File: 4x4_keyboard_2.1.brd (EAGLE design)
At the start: 69.5 x 142.2 mm, 74 parts, among them U2 AMS1117-5.0

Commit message: Routing compelte of uc
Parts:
- moved SV2 3.16 mm to (4.17, 132.3)
- moved LED1 2.37 mm to (20.4, 116.7)
- moved R4 2.24 mm to (22.8, 116.5)
- moved C10 0.74 mm to (24.6, 116.3), turned to 270 degrees
- moved C5 0.62 mm to (28.2, 133.6)
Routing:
- net VCC: track 0.00 -> 82.8 mm
- net SW1: track 0.00 -> 48.9 mm, vias 0 -> 4
- net A1: track 0.00 -> 48.8 mm, vias 0 -> 2
- net A2: track 0.00 -> 47.0 mm, vias 0 -> 4
- net B1: track 0.00 -> 46.9 mm, vias 0 -> 2
- net B2: track 0.00 -> 46.7 mm, vias 0 -> 4
- net RESET: track 0.00 -> 46.5 mm
- net SW3: track 0.00 -> 35.9 mm, vias 0 -> 1
- net SW2: track 0.00 -> 32.4 mm, vias 0 -> 1
- net MISO: track 0.00 -> 27.7 mm, vias 0 -> 2
- net SCK: track 0.00 -> 26.4 mm, vias 0 -> 2
- net MOSI: track 0.00 -> 25.8 mm, vias 0 -> 2
- net V_USB: track 0.00 -> 22.4 mm
- net N$24: track 0.00 -> 17.1 mm
- net N$27: track 0.00 -> 16.7 mm
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
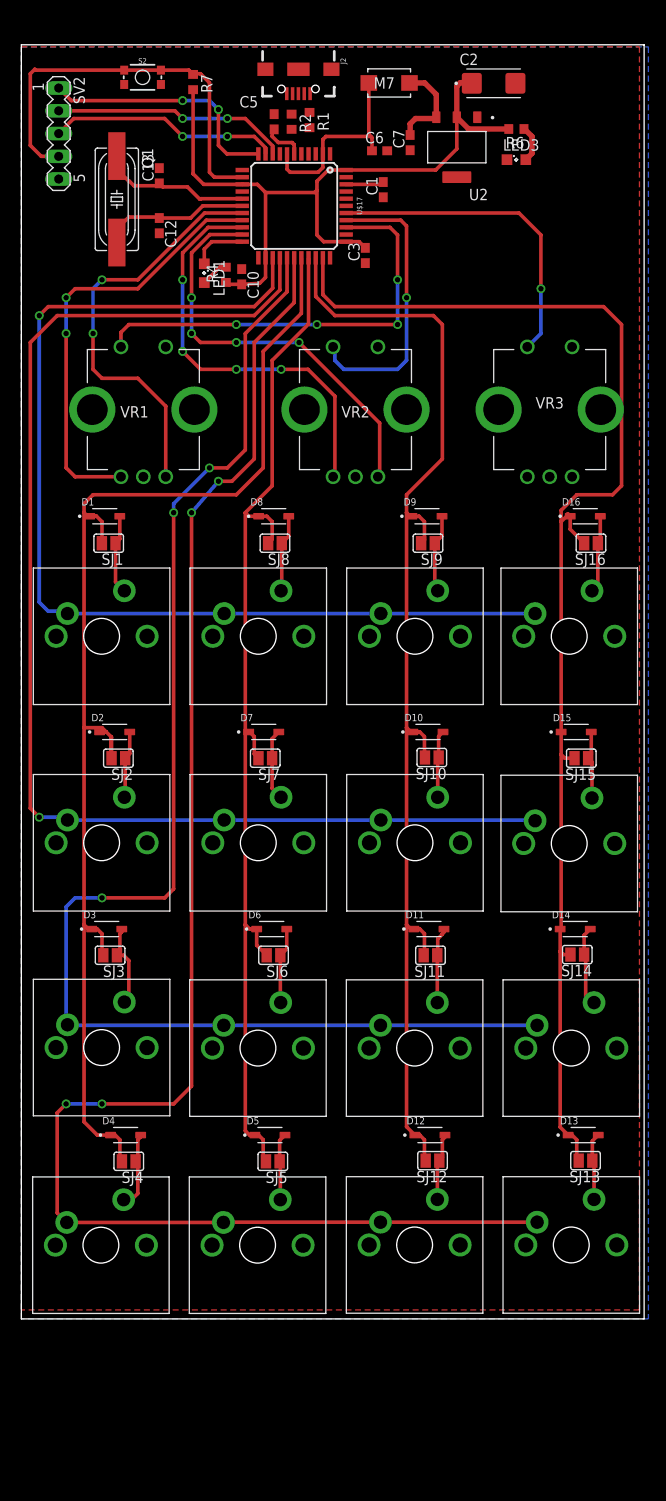
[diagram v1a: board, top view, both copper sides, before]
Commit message: Correct routing signal
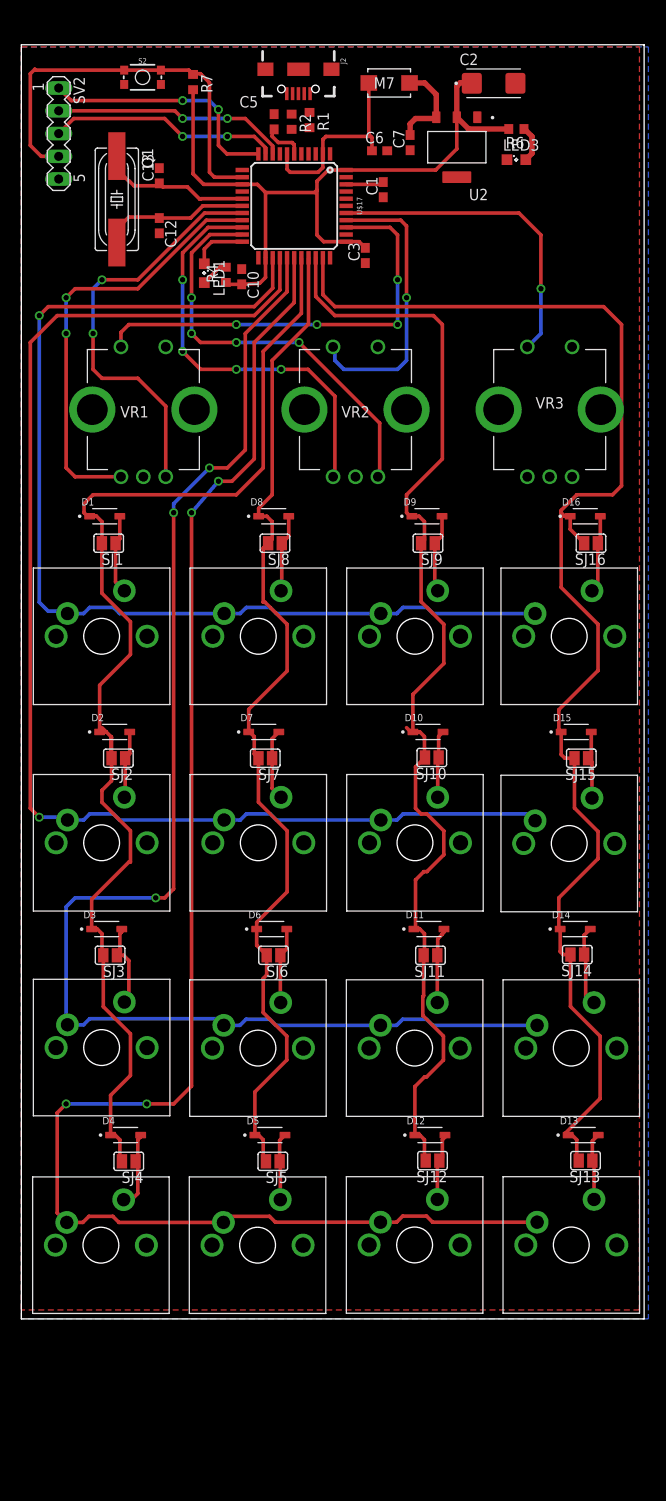
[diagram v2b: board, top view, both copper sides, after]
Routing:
- net COL4: track 146.6 -> 154.9 mm
- net COL1: track 142.0 -> 136.5 mm
- net COL2: track 119.6 -> 114.9 mm
- net COL3: track 130.9 -> 129.2 mm
- net ROW1: track 118.6 -> 120.3 mm
- net ROW3: track 155.4 -> 157.1 mm
- net ROW2: track 142.8 -> 144.5 mm
- net ROW4: track 179.4 -> 181.0 mm

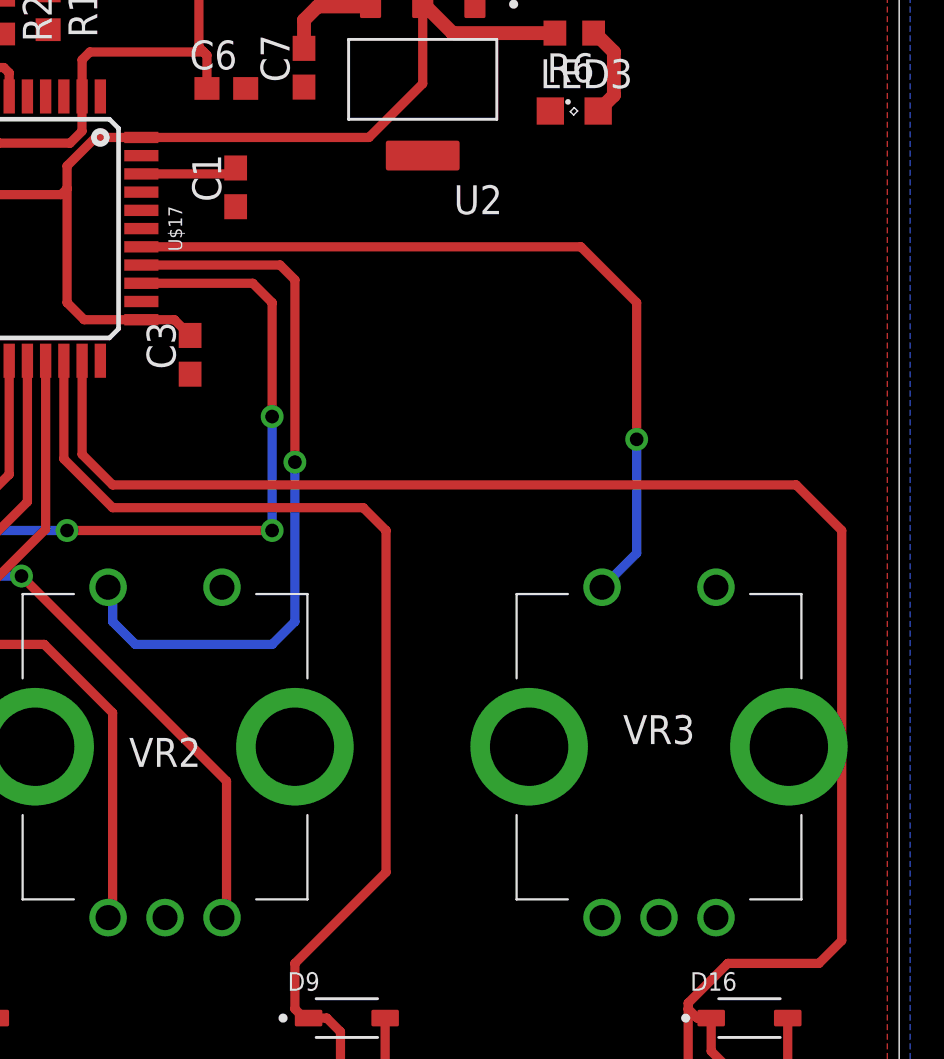
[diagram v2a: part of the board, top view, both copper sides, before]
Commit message: complete the routing of encoder and changer it analogpins
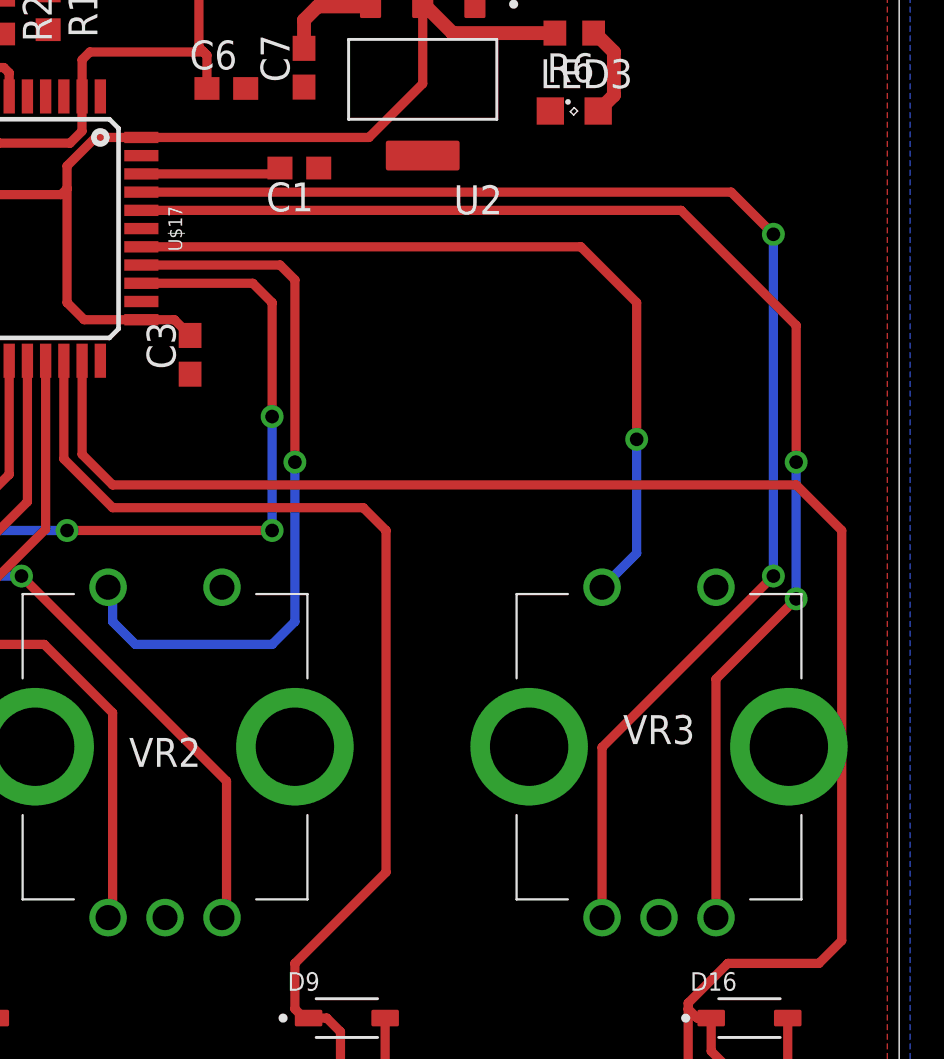
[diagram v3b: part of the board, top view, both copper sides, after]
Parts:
- moved C1 2.92 mm to (43.2, 126.9), turned to 180 degrees
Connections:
- net A3: now also U$17.41; no longer U$17.12
- net B3: now also U$17.40; no longer U$17.8
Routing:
- net A3: track 0.00 -> 61.6 mm, vias 0 -> 2
- net B3: track 0.00 -> 58.3 mm, vias 0 -> 2
- net AREF: track 4.25 -> 6.19 mm
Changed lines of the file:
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@@
 <?xml version="1.0" encoding="utf-8"?>
 <!DOCTYPE eagle SYSTEM "eagle.dtd">
-<eagle version="9.6.2">
+<eagle version="6.4">
 <drawing>
 <settings>
 <setting alwaysvectorfont="no"/>
-<setting keepoldvectorfont="yes"/>
 <setting verticaltext="up"/>
 </settings>
@@
 <param name="dpMaxLengthDifference" value="10mm"/>
 <param name="dpGapFactor" value="2.5"/>
+<param name="checkGrid" value="0"/>
 <param name="checkAngle" value="0"/>
 <param name="checkFont" value="1"/>
 <param name="checkRestrict" value="1"/>
-<param name="checkStop" value="0"/>
-<param name="checkValues" value="0"/>
-<param name="checkNames" value="1"/>
-<param name="checkWireStubs" value="1"/>
-<param name="checkPolygonWidth" value="0"/>
 <param name="useDiameter" value="13"/>
 <param name="maxErrors" value="50"/>
@@
 <pass name="Default">
 <param name="RoutingGrid" value="50mil"/>
-<param name="AutoGrid" value="1"/>
-<param name="Efforts" value="0"/>
-<param name="TopRouterVariant" value="1"/>
 <param name="tpViaShape" value="round"/>
 <param name="PrefDir.1" value="|"/>
@@
 </autorouter>
 <elements>
-<element name="C1" library="rcl" package="C0603" value="0.1uF" x="40.4" y="126.06" smashed="yes" rot="R90">
-<attribute name="NAME" x="39.765" y="125.425" size="1.27" layer="25" rot="R90"/>
-<attribute name="POPULARITY" value="73" x="142" y="154" size="1.778" layer="27" rot="R90" display="off"/>
-<attribute name="SPICEPREFIX" value="C" x="142" y="154" size="1.778" layer="27" rot="R90" display="off"/>
-<attribute name="VALUE" x="42.305" y="125.425" size="1.27" layer="27" rot="R90"/>
+<element name="C1" library="rcl" package="C0603" value="0.1uF" x="43.194" y="126.908" smashed="yes" rot="R180">
+<attribute name="NAME" x="43.829" y="126.273" size="1.27" layer="25" rot="R180"/>
+<attribute name="POPULARITY" value="73" x="15.254" y="228.508" size="1.778" layer="27" rot="R180" display="off"/>
+<attribute name="SPICEPREFIX" value="C" x="15.254" y="228.508" size="1.778" layer="27" rot="R180" display="off"/>
+<attribute name="VALUE" x="43.829" y="128.813" size="1.27" layer="27" rot="R180"/>
 </element>
 <element name="C10" library="rcl" package="C0603" value="1.0uF" x="24.6" y="116.34" smashed="yes" rot="R270">
@@
 <wire x1="30.28" y1="136.775" x2="29.63" y2="136.775" width="0" layer="19" extent="1-1"/>
 <wire x1="28.219" y1="134.49" x2="29.63" y2="136.775" width="0" layer="19" extent="1-1"/>
-<wire x1="36.26" y1="127.45" x2="40.4" y2="125.21" width="0" layer="19" extent="1-1"/>
+<wire x1="36.26" y1="127.45" x2="44.044" y2="126.908" width="0" layer="19" extent="1-1"/>
 </signal>
 <signal name="D-">
@@
 <contactref element="C1" pad="2"/>
 <contactref element="U$17" pad="42"/>
-<wire x1="36.26" y1="126.65" x2="40.14" y2="126.65" width="0.4064" layer="1"/>
-<wire x1="40.14" y1="126.65" x2="40.4" y2="126.91" width="0.4064" layer="1"/>
+<wire x1="36.26" y1="126.65" x2="42.086" y2="126.65" width="0.4064" layer="1"/>
+<wire x1="42.086" y1="126.65" x2="42.344" y2="126.908" width="0.4064" layer="1"/>
 </signal>
 <signal name="RESET">
@@
 <signal name="B3">
 <contactref element="VR3" pad="B1"/>
-<contactref element="U$17" pad="8"/>
-<wire x1="61.48" y1="94.01" x2="28.86" y2="130.05" width="0" layer="19" extent="1-1"/>
+<contactref element="U$17" pad="40"/>
+<wire x1="36.26" y1="125.05" x2="59.95" y2="125.05" width="0.4064" layer="1"/>
+<wire x1="59.95" y1="125.05" x2="65" y2="120" width="0.4064" layer="1"/>
+<wire x1="65" y1="120" x2="65" y2="114" width="0.4064" layer="1"/>
+<via x="65" y="114" extent="1-16" drill="0.6" shape="square"/>
+<wire x1="65" y1="114" x2="65" y2="108" width="0.4064" layer="16"/>
+<wire x1="61.48" y1="94.01" x2="61.48" y2="104.48" width="0.4064" layer="1"/>
+<wire x1="61.48" y1="104.48" x2="65" y2="108" width="0.4064" layer="1"/>
+<via x="65" y="108" extent="1-16" drill="0.6" shape="square"/>
 </signal>
 <signal name="A3">
 <contactref element="VR3" pad="A1"/>
-<contactref element="U$17" pad="12"/>
-<wire x1="24.66" y1="128.25" x2="56.48" y2="94.01" width="0" layer="19" extent="1-1"/>
+<contactref element="U$17" pad="41"/>
+<wire x1="36.26" y1="125.85" x2="62.15" y2="125.85" width="0.4064" layer="1"/>
+<wire x1="56.48" y1="94.01" x2="56.48" y2="101.48" width="0.4064" layer="1"/>
+<wire x1="56.48" y1="101.48" x2="64" y2="109" width="0.4064" layer="1"/>
+<via x="64" y="109" extent="1-16" drill="0.6"/>
+<wire x1="64" y1="109" x2="64" y2="124" width="0.4064" layer="16"/>
+<via x="64" y="124" extent="1-16" drill="0.6"/>
+<wire x1="64" y1="124" x2="62.15" y2="125.85" width="0.4064" layer="1"/>
 </signal>
 <signal name="MISO">
@@
 </signal>
 </signals>
-<mfgpreviewcolors>
-<mfgpreviewcolor name="soldermaskcolor" color="0xC8008000"/>
-<mfgpreviewcolor name="silkscreencolor" color="0xFFFEFEFE"/>
-<mfgpreviewcolor name="backgroundcolor" color="0xFF282828"/>
-<mfgpreviewcolor name="coppercolor" color="0xFFFFBF00"/>
-<mfgpreviewcolor name="substratecolor" color="0xFF786E46"/>
-</mfgpreviewcolors>
 </board>
 </drawing>

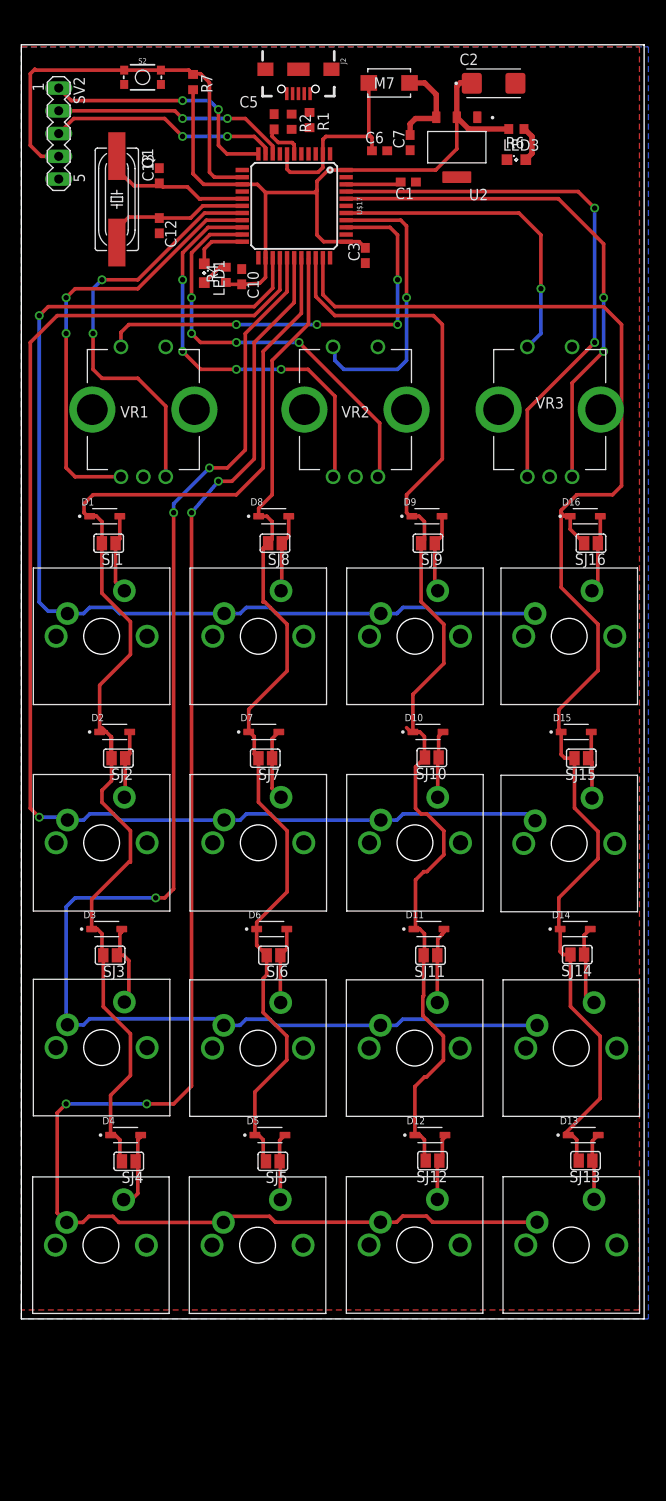
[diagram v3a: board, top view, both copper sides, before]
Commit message: Complete the routing and error free
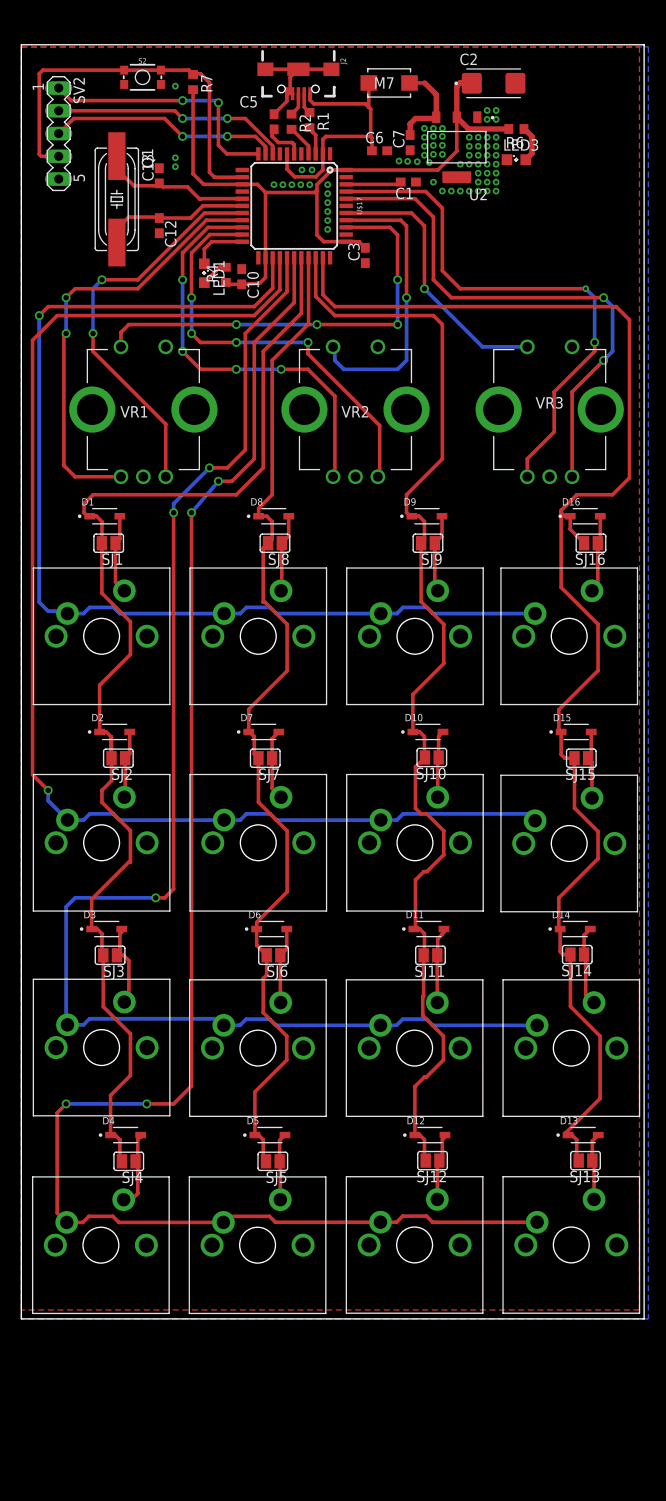
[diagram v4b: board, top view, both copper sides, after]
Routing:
- net GND: track 0.00 -> 14.2 mm, vias 0 -> 67
- net V_USB: track 22.4 -> 30.6 mm
- net SW3: track 35.9 -> 30.5 mm
- net D+: track 0.00 -> 3.55 mm
- net D-: track 0.00 -> 3.22 mm
- net N$3: track 0.00 -> 2.60 mm
- net B1: track 46.9 -> 44.5 mm
- net N$1: track 0.00 -> 2.34 mm
- net ROW2: track 144.5 -> 142.6 mm
- net A3: track 61.6 -> 59.9 mm
- net RESET: track 46.5 -> 45.0 mm
- net B3: track 58.3 -> 59.7 mm
- net COL4: track 154.9 -> 156.3 mm
- net COL3: track 129.2 -> 128.0 mm
- net COL1: track 136.5 -> 135.5 mm
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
